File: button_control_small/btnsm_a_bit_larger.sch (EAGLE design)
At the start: 18 parts, among them IC1 TINY13V-10SSU, Q1 IRF8788

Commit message: Added version for heater canister
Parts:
- added LED1, LED3: (no value), eagle-ltspice:LED_ESML0603
- added LED2, LED4: (no value), led:LED5MM
- added R3: 300, rcl:R-EU_R0402
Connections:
- new net N$6: LED1.A, LED2.A, LED3.A, LED4.A, R3.2
- net N$3: now also R3.1
- net N$4: now also LED1.C, LED2.C, LED3.C, LED4.C
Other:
- moved on the sheet: IN-, OUT-
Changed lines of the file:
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@@
 </variantdefs>
 <classes>
-<class number="0" name="default" width="0" drill="0">
+<class number="0" name="default" width="0.3" drill="0.3">
+<clearance class="0" value="0.1778"/>
 </class>
 </classes>
@@
 <part name="PAD5" library="wirepad" library_urn="urn:adsk.eagle:library:412" deviceset="1,6/0,9" device=""/>
 <part name="PAD6" library="wirepad" library_urn="urn:adsk.eagle:library:412" deviceset="1,6/0,9" device=""/>
+<part name="LED1" library="eagle-ltspice" library_urn="urn:adsk.eagle:library:217" deviceset="LED_E" device="SML0603"/>
+<part name="LED2" library="led" library_urn="urn:adsk.eagle:library:259" deviceset="LED" device="5MM"/>
+<part name="R3" library="rcl" library_urn="urn:adsk.eagle:library:334" deviceset="R-EU_" device="R0402" value="300"/>
+<part name="LED3" library="eagle-ltspice" library_urn="urn:adsk.eagle:library:217" deviceset="LED_E" device="SML0603"/>
+<part name="LED4" library="led" library_urn="urn:adsk.eagle:library:259" deviceset="LED" device="5MM"/>
 </parts>
 <sheets>
@@
 <instance part="C1" gate="G$1" x="20.32" y="58.42"/>
 <instance part="GND5" gate="1" x="20.32" y="50.8"/>
-<instance part="IN-" gate="1" x="35.56" y="45.72"/>
+<instance part="IN-" gate="1" x="12.7" y="33.02" rot="R270"/>
 <instance part="IN+" gate="1" x="76.2" y="58.42"/>
 <instance part="OUT+" gate="1" x="88.9" y="60.96" rot="R270"/>
-<instance part="OUT-" gate="1" x="60.96" y="38.1" rot="R270"/>
-<instance part="GND6" gate="1" x="40.64" y="45.72" rot="R90"/>
+<instance part="OUT-" gate="1" x="50.8" y="38.1" rot="R270"/>
+<instance part="GND6" gate="1" x="12.7" y="27.94"/>
 <instance part="C2" gate="G$1" x="81.28" y="55.88"/>
 <instance part="C3" gate="G$1" x="25.4" y="35.56"/>
@@
 <instance part="PAD5" gate="1" x="86.36" y="86.36"/>
 <instance part="PAD6" gate="1" x="86.36" y="81.28"/>
+<instance part="LED1" gate="G$1" x="66.04" y="50.8"/>
+<instance part="LED2" gate="G$1" x="55.88" y="50.8"/>
+<instance part="R3" gate="G$1" x="60.96" y="58.42" rot="R270"/>
+<instance part="LED3" gate="G$1" x="48.26" y="50.8"/>
+<instance part="LED4" gate="G$1" x="38.1" y="50.8"/>
 </instances>
 <busses>
@@
 <pinref part="C2" gate="G$1" pin="1"/>
 <junction x="81.28" y="58.42"/>
+<pinref part="R3" gate="G$1" pin="1"/>
+<wire x1="60.96" y1="63.5" x2="81.28" y2="63.5" width="0.1524" layer="91"/>
+<wire x1="81.28" y1="63.5" x2="81.28" y2="58.42" width="0.1524" layer="91"/>
 </segment>
 </net>
@@
 <pinref part="Q1" gate="G$1" pin="D"/>
 <pinref part="OUT-" gate="1" pin="P"/>
-</segment>
-</net>
+<wire x1="50.8" y1="35.56" x2="60.96" y2="35.56" width="0.1524" layer="91"/>
+<pinref part="LED1" gate="G$1" pin="C"/>
+<pinref part="LED2" gate="G$1" pin="C"/>
+<wire x1="66.04" y1="45.72" x2="60.96" y2="45.72" width="0.1524" layer="91"/>
+<wire x1="60.96" y1="45.72" x2="55.88" y2="45.72" width="0.1524" layer="91"/>
+<wire x1="60.96" y1="35.56" x2="60.96" y2="45.72" width="0.1524" layer="91"/>
+<junction x="60.96" y="35.56"/>
+<junction x="60.96" y="45.72"/>
+<pinref part="LED4" gate="G$1" pin="C"/>
+<pinref part="LED3" gate="G$1" pin="C"/>
+<wire x1="38.1" y1="45.72" x2="48.26" y2="45.72" width="0.1524" layer="91"/>
+<wire x1="55.88" y1="45.72" x2="48.26" y2="45.72" width="0.1524" layer="91"/>
+<junction x="55.88" y="45.72"/>
+<junction x="48.26" y="45.72"/>
+</segment>
+</net>
+<net name="N$6" class="0">
+<segment>
+<pinref part="LED4" gate="G$1" pin="A"/>
+<pinref part="LED3" gate="G$1" pin="A"/>
+<wire x1="38.1" y1="53.34" x2="48.26" y2="53.34" width="0.1524" layer="91"/>
+<pinref part="LED1" gate="G$1" pin="A"/>
+<pinref part="LED2" gate="G$1" pin="A"/>
+<wire x1="66.04" y1="53.34" x2="60.96" y2="53.34" width="0.1524" layer="91"/>
+<pinref part="R3" gate="G$1" pin="2"/>
+<wire x1="60.96" y1="53.34" x2="55.88" y2="53.34" width="0.1524" layer="91"/>
+<junction x="60.96" y="53.34"/>
+<wire x1="48.26" y1="53.34" x2="55.88" y2="53.34" width="0.1524" layer="91"/>
+<junction x="48.26" y="53.34"/>
+<junction x="55.88" y="53.34"/>
+</segment>
+</net>

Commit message: Add files via upload
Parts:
- removed IC1: TINY13V-10SSU, atmel:TINY13V-10SSU
- removed LED1, LED3: (no value), eagle-ltspice:LED_ESML0603
- removed LED2, LED4: (no value), led:LED5MM
- removed PAD1, PAD2, PAD3, PAD4, PAD5, PAD6: (no value), wirepad:1,6/0,9
- added BTN1: BTN1, wirepad:1,6/0,9
- added BTN2: BNT2, wirepad:1,6/0,9
- added C4, C5: 100n, resistor:C-EUC0603
- added D1: (no value), SparkFun-LED:LED-RGBNO_IC
- added IC2: MEGA8-AI, atmel:MEGA8-AI
- added J1: AVR_SPI_PROG_3X2NS, SparkFun-Connectors:AVR_SPI_PROG_3X2NS
- added R10: 100k, rcl:R-EU_R0402
- added R4, R5: 470, rcl:R-EU_R0402
- added R6: 520, rcl:R-EU_R0402
- added R7: 282k, rcl:R-EU_R0402
- added R8: 470k, rcl:R-EU_R0402
- added R9: 2.2k, rcl:R-EU_R0402
- added RX: RX, wirepad:1,6/0,9
- added T1, T2: BC848, transistor-neu-to92:BC848
- added TX: TX, wirepad:1,6/0,9
- added WTR: WATER, wirepad:1,6/0,9
- C2: value 0.33uF -> 100n
- C3: value 2.2uF -> 1uF; device resistor:C-EUC0603 -> resistor:C-EUC0805
- R3: value 300 -> 100k
- U$3: value TPS71550 -> TPS71533
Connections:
- removed net N$1: IC1.PB4/PCINT4/ADC2, R1.2
- removed net N$3: C2.1, IN+.P, OUT+.P, R3.1, U$3.IN
- new net ADC0: IC2.PC0(ADC0), R3.1, R7.2
- new net AREF: C5.2, IC2.AREF
- new net BTN1: BTN1.P, IC2.PD2(INT0)
- new net N$13: T1.E, T2.B
- new net N$16: R10.2, R8.1, WTR.P
- new net N$17: R10.1, T1.B
- new net N$18: R9.1, T1.C
- new net N$7: D1.GRN-C, R4.2
- new net N$8: D1.BLU-C, R5.2
- new net PWM0: D1.BLU-A, IC2.PD6(AIN0)
- new net PWM1: D1.GRN-A, IC2.PB2(SS/OC1B)
- new net PWM2: D1.RED-A, IC2.PB1(OC1A)
- new net RX: IC2.PD0(RXD), R1.2, RX.P
- new net TX: IC2.PD1(TXD), TX.P
- new net VIN: C2.1, IN+.P, OUT+.P, R4.1, R5.1, R6.1, R7.1, R9.2, U$3.IN
- new net WTR: IC2.PD3(INT1), T2.C
- net GND: now also BTN2.P, C4.2, C5.1, IC2.GND, IC2.GND@1, IC2.GND@2, J1.6, R8.2, T2.E; no longer IC1.GND, PAD6.P
- net MISO: now also IC2.PB4(MISO), J1.1; no longer IC1.PB1/PCINT1/AIN1/OC0B/INT0/MISO, PAD2.P
- net MOSI: now also IC2.PB3(MOSI/OC2), J1.4; no longer IC1.PB0/PCINT0/AIN0/OC0A/MOSI, PAD1.P
- net N$4: now also R3.2; no longer LED1.C, LED2.C, LED3.C, LED4.C
- net N$6: now also D1.RED-C, R6.2; no longer LED1.A, LED2.A, LED3.A, LED4.A, R3.2
- net RST: now also IC2.PC6(/RESET), J1.5; no longer IC1.PB5/PCINT5/!RESET!/ADC0/DW, PAD4.P
- net SCK: now also IC2.PB5(SCK), J1.3; no longer IC1.PB2/PCINT2/SCK/ADC1/T0, PAD3.P
- net VDD: now also C4.1, IC2.AVCC, IC2.VCC@1, IC2.VCC@2, J1.2; no longer IC1.VCC, PAD5.P
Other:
- moved on the sheet: C1, C2, IN+, OUT+, OUT-, Q1, R1, R2, R3, U$3

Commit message: Add files via upload
Developing a new version with better power consumption and capabilities
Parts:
- removed OUT-: OUT-, wirepad:SMD5
- removed RX: RX, wirepad:1,6/0,9
- removed TX: TX, wirepad:1,6/0,9
- added D2: (no value), SparkFun-LED:LED-RGBNO_IC
- added D3: BAT54, diode:BAT54
- added J2: OUT-, SparkFun-Connectors:CONN_01PTH_2MM
- added J3: OUT+, SparkFun-Connectors:CONN_01PTH_2MM
- added Q2, Q3, Q5: IRLML9301, SparkFun-DiscreteSemi:MOSFET_PCH-IRLML2244
- added Q4: 2N2007 (SOT323), SparkFun-DiscreteSemi:MOSFET-NCH-2N7002PW
- added R11, R12: 470, rcl:R-EU_R0805
- added R13: 520, rcl:R-EU_R0805
- added R14, R15, R16, R17, R20, R21, R22, R23, R28, R29, R30: 100k, rcl:R-EU_R0402
- added R18, R19, R24, R25, R26, R27: 200, rcl:R-EU_R0402
- added T3, T4, T5: BC848, transistor-neu-to92:BC848
- added U$1: IRFH6200, IRFH6200:IRFH6200
- added U1: ACS711ELCTR-25AB-T, allegro:ACS711ELCTR-25AB-T
- added U2: HC_05, Bluetooth HC-05:HC_05
- added WTR1: WTR-PWR, wirepad:1,6/0,9
- D1: value (none) -> BAT54; device SparkFun-LED:LED-RGBNO_IC -> diode:BAT54
- Q1: value IRF8788 -> 2N2007 (SOT323); device transistor-fet:FDS5680 -> SparkFun-DiscreteSemi:MOSFET-NCH-2N7002PW
- R1: value 100R -> 100k
- R2: value 10K -> 282k
- R4: value 470 -> 100k
- R5: value 470 -> 200
- R6: value 520 -> 200
- R7: value 282k -> 100k
- WTR: value WATER -> WTR-IN
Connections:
- removed net ADC0: IC2.PC0(ADC0), R3.1, R7.2
- removed net PWM1: D1.GRN-A, IC2.PB2(SS/OC1B)
- removed net PWM2: D1.RED-A, IC2.PB1(OC1A)
- removed net RX: IC2.PD0(RXD), R1.2, RX.P
- removed net TX: IC2.PD1(TXD), TX.P
- removed net VIN: C2.1, IN+.P, OUT+.P, R4.1, R5.1, R6.1, R7.1, R9.2, U$3.IN
- new net +12V: C2.1, IN+.P, OUT+.P, Q5.S, R11.1, R12.1, R13.1, R21.2, R27.1, R9.2, U$3.IN, WTR1.P
- new net N$1: D2.RED-A, R13.2
- new net N$10: Q4.G, R16.1, R18.2, R6.1
- new net N$11: C1.2, Q5.G, R21.1
- new net N$12: Q4.D, R17.2
- new net N$14: C1.1, IC2.PC1(ADC1)
- new net N$15: D1.A, R18.1
- new net N$19: D3.A, R19.1
- new net N$20: D1.C, D3.C, R20.1, U$1.G
- new net N$21: IC2.PC2(ADC2), R19.2
- new net N$22: IC2.PC0(ADC0), R2.2, R4.1
- new net N$23: Q5.D, R2.1
- new net N$24: D2.BLU-C, T5.C
- new net N$25: D2.GRN-C, T4.C
- new net N$26: D2.RED-C, T3.C
- new net N$27: R23.1, R26.2, T5.B
- new net N$28: R22.1, R25.2, T4.B
- new net N$29: R24.2, R7.1, T3.B
- new net N$3: D2.BLU-A, R11.2
- new net N$30: IC2.PB2(SS/OC1B), R24.1
- new net N$31: IC2.PB1(OC1A), R25.1
- new net N$32: Q3.S, R14.2, R27.2
- new net N$33: Q2.G, R28.1
- new net N$34: J2.1, U1.IP+1, U1.IP+2
- new net N$35: R29.2, R30.1
- new net N$36: Q2.D, R29.1, U1.VCC
- new net N$37: U1.VOUT
- new net N$5: D2.GRN-A, R12.2
- new net N$9: Q3.D, R15.1, R6.2
- net GND: now also Q4.S, R15.2, R16.2, R20.2, R22.2, R23.2, R3.1, R30.2, R4.2, R7.2, T3.E, T4.E, T5.E, U$1.S, U1.GND; no longer C1.2, R8.2, T2.E
- net N$2: now also T2.C; no longer Q1.G
- net N$4: now also R8.2, T2.E; no longer OUT-.P, R3.2
- net N$6: now also Q1.G, R3.2, R5.1; no longer D1.RED-C, R6.2
- net N$7: now also Q3.G, R14.1, U$1.D, U1.IP-1, U1.IP-2; no longer D1.GRN-C, R4.2
- net N$8: no longer D1.BLU-C
- net PWM0: now also R26.1; no longer D1.BLU-A
- net RST: no longer C1.1, R2.1
- net VDD: now also Q2.S, R1.2, R17.1, R28.2; no longer R2.2
- net WTR: no longer T2.C
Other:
- note added: "Вход с МК - включение измерителя"
- note added: "Выход на МК - можно без прерывания"
- note added: "К МК - на прерывание INT1"
- note added: "в выходу мк, который управляем активацией АЦП должны быть импульсы по примерно 2мс"
- note added: "вход с платы (ответный электрод на воду)"
- note added: "к входу АЦП"
- note added: "к выходу основного транзистора для детекции подключения внешнего источника питания"
- note added: "объединение через диоды - чтобы выход включался сам либо по наличию внешнего напряжения либо по сигналу МК"
- moved on the sheet: C1, C2, IN+, OUT+, R1, R10, R2, R3, R4, R5, R6, R7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

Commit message: Add files via upload
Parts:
- removed OUT+: OUT+, wirepad:SMD5
- removed U2: HC_05, Bluetooth HC-05:HC_05
- added C6: 10uF, resistor:C-EUC0805
- added JDY-08: JDY-08, jdy-08:JDY-08
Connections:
- removed net N$2: R1.1, T2.C
- removed net N$8: R5.2
- removed net WTR: IC2.PD3(INT1)
- new net ADC5: IC2.PC5(ADC5/SCL), Q2.G, R28.1
- new net ADC6: IC2.ADC6, U1.VOUT
- new net ADC7: IC2.ADC7, R29.2, R30.1
- new net N$38: IC2.PD0(RXD), JDY-08.P03_TXD
- new net N$39: IC2.PD1(TXD), JDY-08.P02_RXD
- new net PB6: IC2.PB6(XTAL1/TOSC1), R1.1, T2.C
- new net PB7: IC2.PB7(XTAL2/TOSC2), R5.2
- net +12V: now also J3.1; no longer OUT+.P
- net GND: now also C6.2, JDY-08.GND
- net N$12: now also IC2.PD3(INT1)
- net N$33: now also IC2.PC3(ADC3), JDY-08.RST; no longer Q2.G, R28.1
- net N$35: now also IC2.PC4(ADC4/SDA), JDY-08.P00_PWRC; no longer R29.2, R30.1
- net N$37: now also IC2.PD4(XCK/T0), JDY-08.P16(STATUS); no longer U1.VOUT
- net VDD: now also C6.1, JDY-08.VCC
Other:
- note added: "выключатель питания для измерителя"
- moved on the sheet: C1, C4, C5, D1, D3, J2, J3, Q1, Q2, Q3, Q4, Q5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

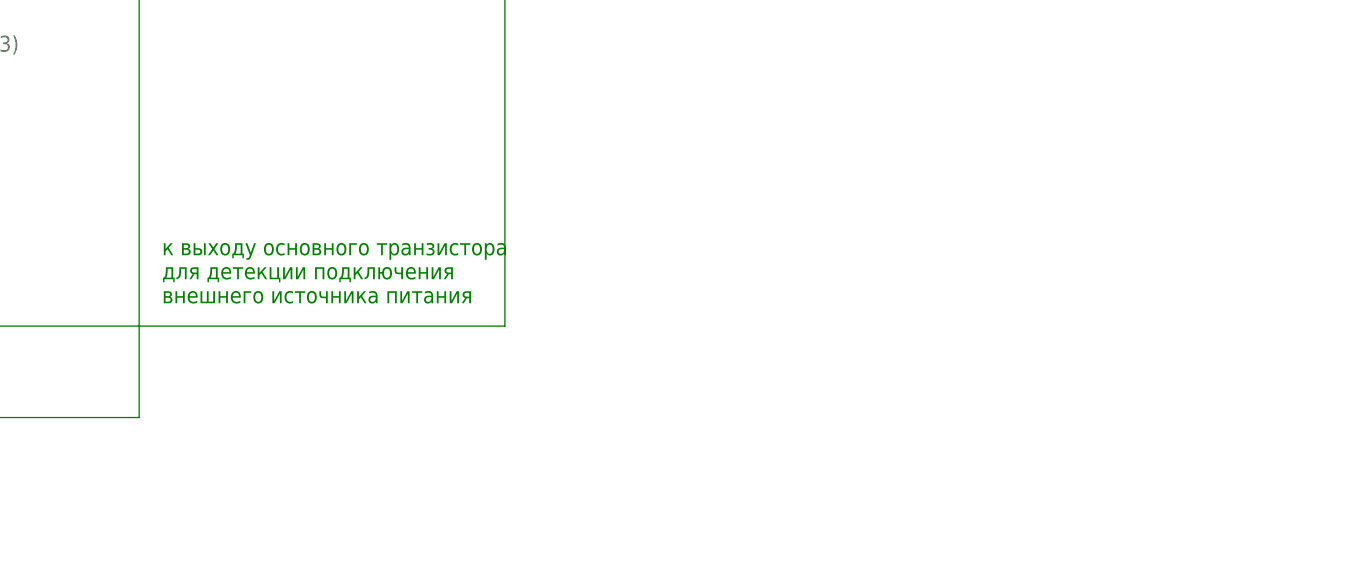
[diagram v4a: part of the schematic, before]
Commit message: Routed version with BT module
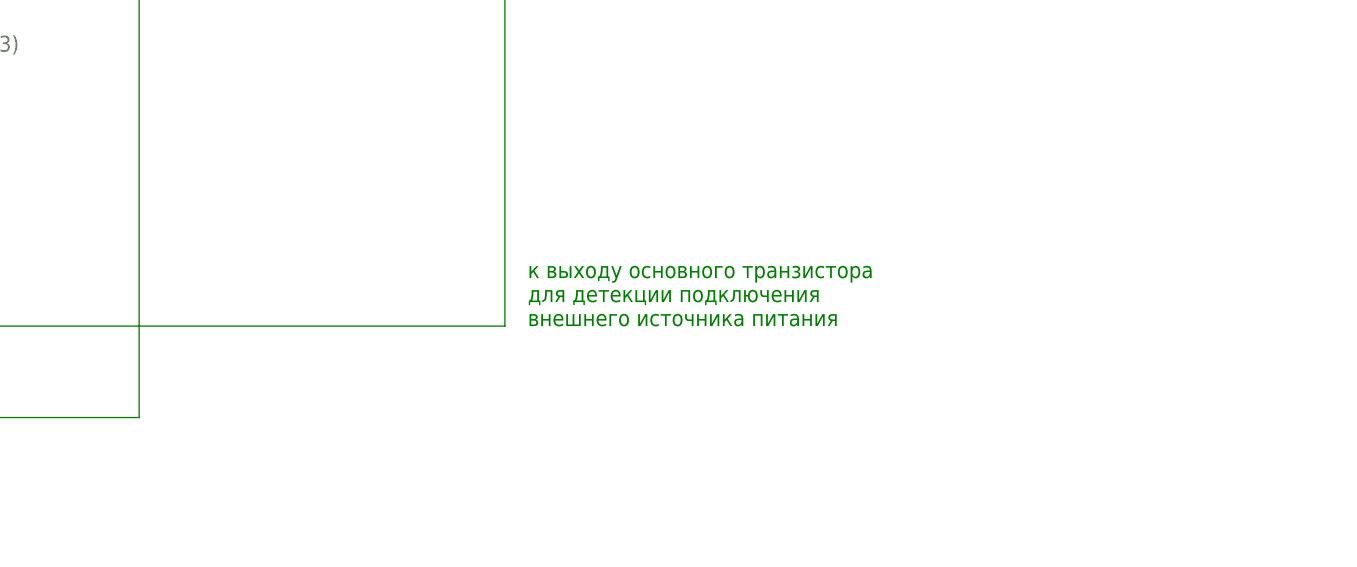
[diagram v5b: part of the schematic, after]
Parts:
- C4, C5: device resistor:C-EUC0603 -> resistor:C-EUC0402
- T2: SPICEPREFIX (none) -> Q
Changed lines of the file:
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@@
 <part name="BTN1" library="wirepad" library_urn="urn:adsk.eagle:library:412" deviceset="1,6/0,9" device="" package3d_urn="urn:adsk.eagle:package:30840/1" value="BTN1"/>
 <part name="CLONE2" library="supply1" library_urn="urn:adsk.eagle:library:371" deviceset="VDD" device=""/>
-<part name="C4" library="resistor" library_urn="urn:adsk.eagle:library:348" deviceset="C-EU" device="C0603" package3d_urn="urn:adsk.eagle:package:26138/1" value="100n"/>
+<part name="C4" library="resistor" library_urn="urn:adsk.eagle:library:348" deviceset="C-EU" device="C0402" package3d_urn="urn:adsk.eagle:package:26136/1" value="100n"/>
 <part name="GND11" library="supply1" library_urn="urn:adsk.eagle:library:371" deviceset="GND" device=""/>
-<part name="C5" library="resistor" library_urn="urn:adsk.eagle:library:348" deviceset="C-EU" device="C0603" package3d_urn="urn:adsk.eagle:package:26138/1" value="100n"/>
+<part name="C5" library="resistor" library_urn="urn:adsk.eagle:library:348" deviceset="C-EU" device="C0402" package3d_urn="urn:adsk.eagle:package:26136/1" value="100n"/>
 <part name="GND13" library="supply1" library_urn="urn:adsk.eagle:library:371" deviceset="GND" device=""/>
 <part name="T1" library="transistor-neu-to92" library_urn="urn:adsk.eagle:library:397" deviceset="BC848" device="" package3d_urn="urn:adsk.eagle:package:28738/1"/>
-<part name="T2" library="transistor-neu-to92" library_urn="urn:adsk.eagle:library:397" deviceset="BC848" device="" package3d_urn="urn:adsk.eagle:package:28738/1"/>
+<part name="T2" library="transistor-neu-to92" library_urn="urn:adsk.eagle:library:397" deviceset="BC848" device="" package3d_urn="urn:adsk.eagle:package:28738/1">
+<attribute name="SPICEPREFIX" value="Q"/>
+</part>
 <part name="R8" library="rcl" library_urn="urn:adsk.eagle:library:334" deviceset="R-EU_" device="R0402" package3d_urn="urn:adsk.eagle:package:23547/1" value="470k"/>
 <part name="R9" library="rcl" library_urn="urn:adsk.eagle:library:334" deviceset="R-EU_" device="R0402" package3d_urn="urn:adsk.eagle:package:23547/1" value="2.2k"/>
@@
 <text x="2.54" y="220.98" size="1.778" layer="91">Выход на МК - можно без прерывания</text>
 <text x="91.44" y="218.44" size="1.778" layer="91">вход с платы (ответный электрод на воду)</text>
-<text x="251.46" y="142.24" size="1.778" layer="91">к выходу основного транзистора
+<text x="292.1" y="139.7" size="1.778" layer="91">к выходу основного транзистора
 для детекции подключения
 внешнего источника питания</text>

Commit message: Switched to HC-05
Added protection for water-input
Added separate power supply for BT & DS18B20
Added DS18B20
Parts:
- removed D3: BAT54, diode:BAT54
- removed JDY-08: JDY-08, jdy-08:JDY-08
- removed WTR: WTR-IN, wirepad:1,6/0,9
- removed WTR1: WTR-PWR, wirepad:1,6/0,9
- added +12: +12, wirepad:WIREPADSMD1,27-254
- added 3V3_CONST: 3V_SW, wirepad:WIREPADSMD1,27-254
- added 3V3_SWITCHED: 3V3, wirepad:WIREPADSMD1,27-254
- added C10: 16pF, resistor:C-EUC0402
- added C7, C8: 1uF, resistor:C-EUC0805
- added C9: 10uF, resistor:C-EUC0805
- added PAD2: WTR_IN, wirepad:WIREPADSMD1,27-254
- added Q6: 3.6864MHz, adafruit:CRYSTALHC49S
- added R31: 4.7k, rcl:R-EU_R0402
- added U$4: MCP1804, 1804:MCP1804
- added U2: HC_05, Bluetooth HC-05:HC_05
- added U3: DS18B20, SparkFun-Sensors:DS18B20
- C1: device resistor:C-EUC0603 -> resistor:C-EUC0603K
- C6: value 10uF -> 16pF; device resistor:C-EUC0805 -> resistor:C-EUC0402
- D1: value BAT54 -> BZX84CSMD; device diode:BAT54 -> diode:BZX84CSMD
- Q1, Q4: value 2N2007 (SOT323) -> 310mA/60V/1.6Ω
- Q2, Q3, Q5: value IRLML9301 -> 4.3A/20V/54mΩ
- R18: value 200 -> 10k
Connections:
- net N$1 renamed R+
- net N$12 renamed PD3
- net N$14 renamed PC1
- net N$18 renamed WTR_MEASURE_PULLUP
- net N$21 renamed PC2
- net N$22 renamed PC0
- net N$24 renamed B-
- net N$25 renamed G-
- net N$26 renamed R-
- net N$27 renamed B-BASE
- net N$28 renamed G-BASE
- net N$29 renamed R-BASE
- net N$3 renamed B+
- net N$30 renamed PB2
- net N$31 renamed PB1
- net N$36 renamed PWR_MEASURE_VCC
- net N$5 renamed G+
- net N$6 renamed WTR_MEASURE_ON
- net N$7 renamed GND_OUT_MEASURE
- net PWM0 renamed PD6(PWM0)
- removed net N$10: Q4.G, R16.1, R18.2, R6.1
- removed net N$15: D1.A, R18.1
- removed net N$16: R10.2, R8.1, WTR.P
- removed net N$19: D3.A, R19.1
- removed net N$20: D1.C, D3.C, R20.1, U$1.G
- removed net N$33: IC2.PC3(ADC3), JDY-08.RST
- removed net N$34: J2.1, U1.IP+1, U1.IP+2
- removed net N$35: IC2.PC4(ADC4/SDA), JDY-08.P00_PWRC
- removed net N$37: IC2.PD4(XCK/T0), JDY-08.P16(STATUS)
- removed net N$38: IC2.PD0(RXD), JDY-08.P03_TXD
- removed net N$39: IC2.PD1(TXD), JDY-08.P02_RXD
- new net GND_OUT: J2.1, R18.2, U1.IP+1, U1.IP+2
- new net OUT_BASE: Q4.G, R16.1, R19.1, R20.1, R6.1, U$1.G
- new net PB0: IC2.PB0(ICP), R31.1, U3.DQ
- new net PC3: D1.C, IC2.PC3(ADC3), R1.1, T2.C
- new net PC4: IC2.PC4(ADC4/SDA), R5.2
- new net PD4-HC05_KEY: IC2.PD4(XCK/T0), U2.PIO11
- new net PD5-HC05_RST: IC2.PD5(T1), U2.RST
- new net PD7: IC2.PD7(AIN1), U$4.!SHDN
- new net RX(UC): IC2.PD0(RXD), U2.TX
- new net TX(UC): IC2.PD1(TXD), U2.RX
- new net VCC: 3V3_SWITCHED.P, C8.1, C9.1, R31.2, U$4.OUT, U2.3V3, U3.VDD
- new net WTR-IN: PAD2.P, R10.2, R8.1
- net +12V: now also +12.P, C7.1, R18.1, U$4.IN; no longer WTR1.P
- net GND: now also C10.1, C6.1, C7.2, C8.2, C9.2, D1.A, U$4.GND, U2.GND, U2.GND1, U2.GND2, U3.GND; no longer C6.2, JDY-08.GND
- net PB6: now also C6.2, Q6.2; no longer R1.1, T2.C
- net PB7: now also C10.2, Q6.1; no longer R5.2
- net VDD: now also 3V3_CONST.P; no longer C6.1, JDY-08.VCC
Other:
- note removed: "вход с платы (ответный электрод на воду)"
- note removed: "выключатель питания для измерителя"
- note removed: "объединение через диоды - чтобы выход включался сам либо по наличию внешнего напряжения либо по сигналу МК"
- moved on the sheet: C4, C5, C6, R18, R5

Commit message: Removed extra wire
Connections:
- new net N$1: Q4.G, R16.1, R6.1
- net OUT_BASE: no longer Q4.G, R16.1, R6.1
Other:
- moved on the sheet: C2, C7, C8, IN+, J2, J3, Q2, Q3, Q4, R14, R15, R16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

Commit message: Added FRAM and extra capacitors
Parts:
- removed +12: +12, wirepad:WIREPADSMD1,27-254
- removed D1: BZX84CSMD, diode:BZX84CSMD
- removed R29, R30: 100k, rcl:R-EU_R0402
- removed U$4: MCP1804, 1804:MCP1804
- added C11, C13, C14, C16: 10n, resistor:C-EUC0402
- added C12, C15: 100n, resistor:C-EUC0402
- added C17: 1uF, resistor:C-EUC0805
- added IC1: LP298XS, adafruit:LP298XS
- added IC3: FM24-SG, ramtron-2:FM24-SG
- added R32: 10k, rcl:R-EU_R0402
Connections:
- removed net ADC5: IC2.PC5(ADC5/SCL), Q2.G, R28.1
- removed net MISO: IC2.PB4(MISO), J1.1
- removed net PC4: IC2.PC4(ADC4/SDA), R5.2
- new net N$2: C11.1, IC1.BYP
- new net PB4/MISO: IC2.PB4(MISO), J1.1, R5.2
- new net SCL: IC2.PC5(ADC5/SCL), IC3.SCL
- new net SDA: IC2.PC4(ADC4/SDA), IC3.SDA
- net +12V: now also IC1.VIN; no longer +12.P, U$4.IN
- net ADC7: now also R2.2, R4.1; no longer R29.2, R30.1
- net AREF: now also C14.1
- net GND: now also C11.2, C12.2, C13.2, C14.2, C15.2, C16.2, C17.2, IC1.GND, IC3.GND; no longer D1.A, R30.2, U$4.GND
- net PC0: now also Q2.G, R28.1; no longer R2.2, R4.1
- net PC3: no longer D1.C
- net PD7: now also IC1.EN; no longer U$4.!SHDN
- net PWR_MEASURE_VCC: no longer R29.1
- net RST: now also C12.1, R32.1
- net VCC: now also C15.1, C16.1, C17.1, IC1.VOUT, IC3.VCC; no longer U$4.OUT
- net VDD: now also C13.1, R32.2
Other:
- note removed: "К МК - на прерывание INT1"
- note removed: "к входу АЦП"
- note removed: "к выходу основного транзистора для детекции подключения внешнего источника питания"
